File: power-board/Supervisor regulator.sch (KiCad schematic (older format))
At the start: 8 parts, among them U3 TPS7A4101

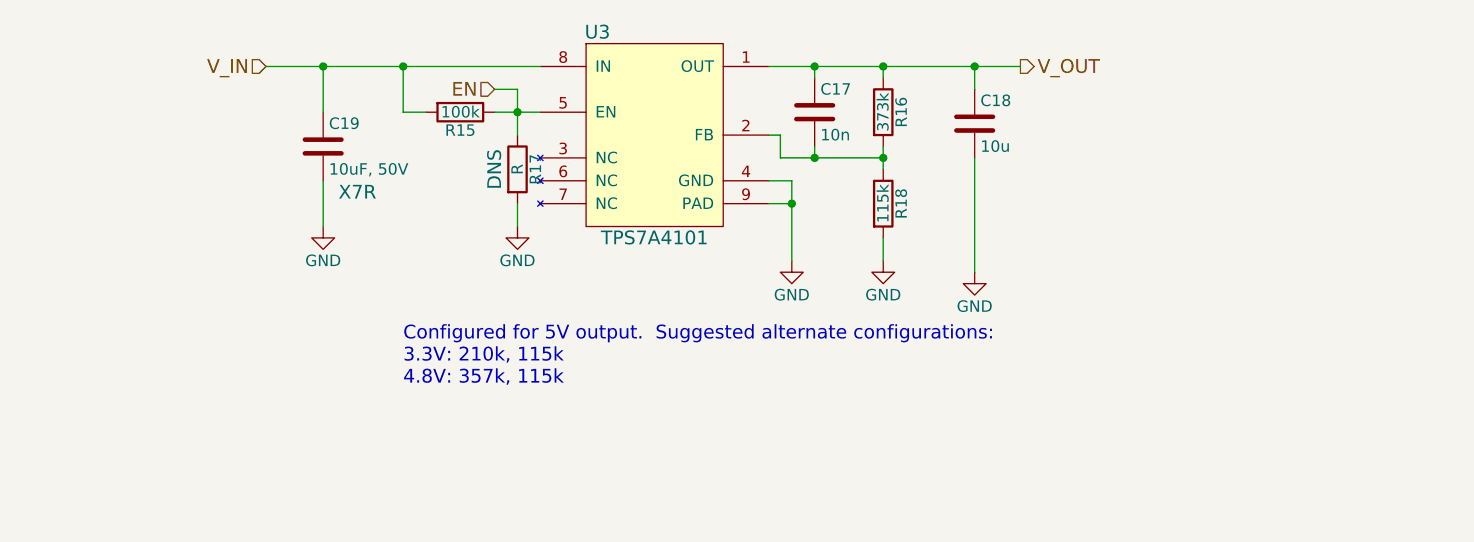
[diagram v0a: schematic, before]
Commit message: changed MCU to run at 3.3v
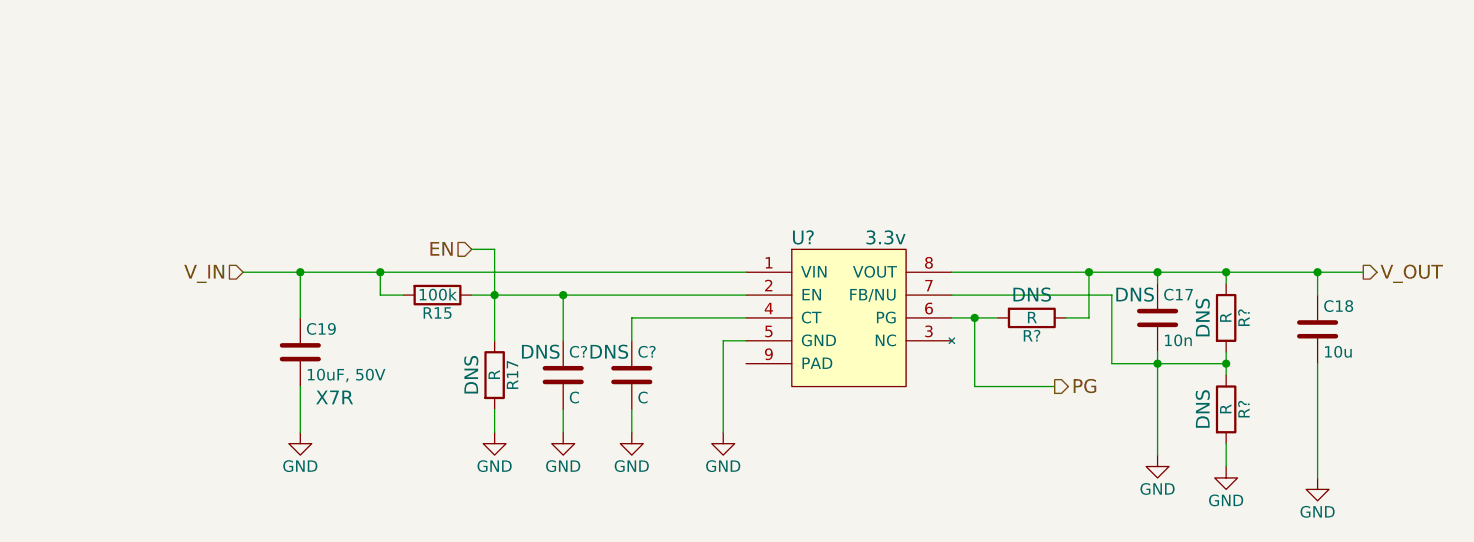
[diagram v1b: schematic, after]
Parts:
- removed R16: 373k, symbol R
- removed R18: 115k, symbol R
- removed U3: TPS7A4101, symbol TPS7A4101
- added C? (x2): C, symbol C
- added R? (x3): R, symbol R
- added U?: 3.3v, symbol TPS7A66xx-Q1
- C17: Note (none) -> DNS
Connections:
- net EN: now also C?.1, U?.2 (EN)
- net GND: now also C17.2, C?.2, C?.2, R?.1, R?.2, R?.2, U?.5 (GND), U?.7 (FB/NU)
- net V_IN: now also U?.1 (VIN)
- net V_OUT: now also R?.1, R?.1, U?.8 (VOUT)
- new net: C?.1, U?.4 (CT)
- new net PG: R?.2, U?.6 (PG)
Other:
- note removed: "Configured for 5V output. Suggested alternate configurations:\n3.3V: 210k, 115k\n4.8V: 357k, 115k"
- moved on the sheet: C17, C18, C19, R15, R17

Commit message: switched to XMEGA A4U
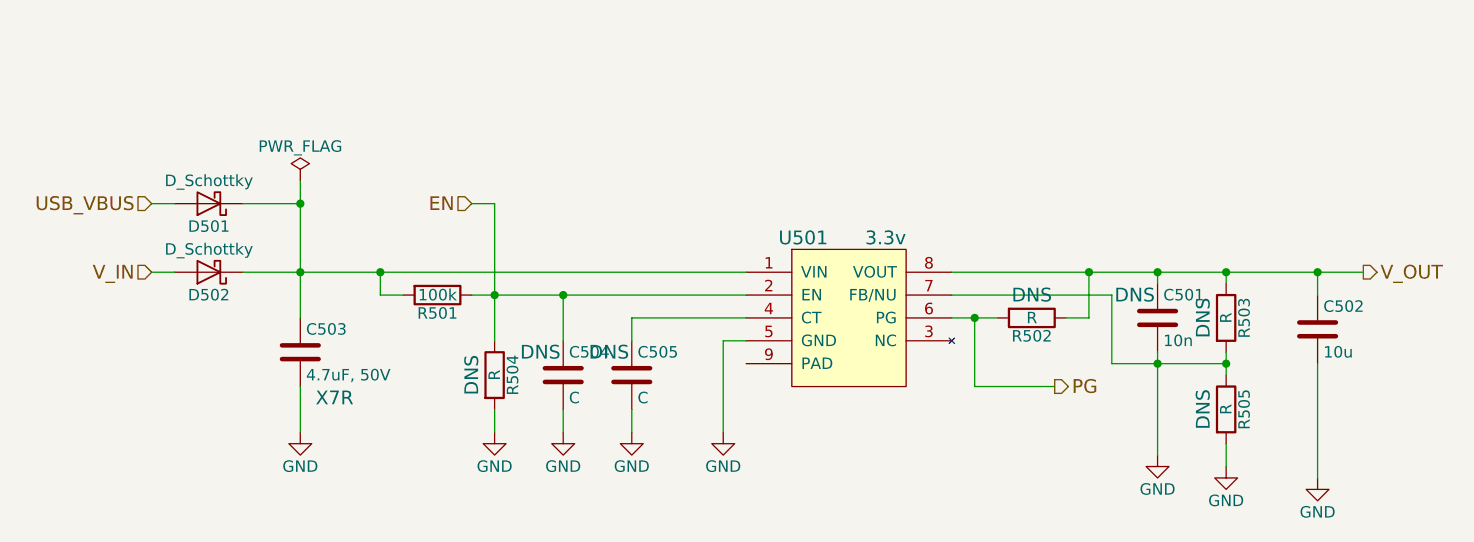
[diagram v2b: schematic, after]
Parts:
- added D501, D502: D_Schottky, symbol D_Schottky
- C503: renamed from C19; value 10uF, 50V -> 4.7uF, 50V; MFG Samsung -> (none); MPN CL31B106KBHNNNE -> (none)
- gave numbers to parts that had none: 6
- renumbered C17 to C501, C18 to C502, R15 to R501, R17 to R504
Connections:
- net V_IN: now also D502.2 (A); no longer C503.1, R501.2, U501.1 (VIN)
- new net: C503.1, D501.1 (K), D502.1 (K), R501.2, U501.1 (VIN)
- new net USB_VBUS: D501.2 (A)
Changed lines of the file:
@@
 $Descr A4 11693 8268
 encoding utf-8
-Sheet 5 10
+Sheet 5 11
 Title ""
 Date ""
@@
 Text HLabel 8100 3300 2    60   Output ~ 0
 V_OUT
-Text HLabel 3200 3300 0    60   Input ~ 0
+Text HLabel 2800 3300 0    60   Input ~ 0
 V_IN
 $Comp
-L C C19
+L C C503
 U 1 1 59357AE9
 P 3450 3650
-F 0 "C19" H 3475 3750 50  0000 L CNN
-F 1 "10uF, 50V" H 3475 3550 50  0000 L CNN
+F 0 "C503" H 3475 3750 50  0000 L CNN
+F 1 "4.7uF, 50V" H 3475 3550 50  0000 L CNN
 F 2 "" H 3488 3500 50  0000 C CNN
 F 3 "" H 3450 3650 50  0000 C CNN
 F 4 "X7R" H 3600 3450 60  0000 C CNN "Note"
-F 5 "Samsung" H 3450 3650 60  0001 C CNN "MFG"
-F 6 "CL31B106KBHNNNE" H 3450 3650 60  0001 C CNN "MPN"
 	1    3450 3650
 	1    0    0    -1
 $EndComp
 $Comp
-L C C17
+L C C501
 U 1 1 59357B30
 P 7200 3500
-F 0 "C17" H 7225 3600 50  0000 L CNN
+F 0 "C501" H 7225 3600 50  0000 L CNN
 F 1 "10n" H 7225 3400 50  0000 L CNN
 F 2 "" H 7238 3350 50  0000 C CNN
@@
 $EndComp
 $Comp
-L C C18
+L C C502
 U 1 1 59357B4B
 P 7900 3550
-F 0 "C18" H 7925 3650 50  0000 L CNN
+F 0 "C502" H 7925 3650 50  0000 L CNN
 F 1 "10u" H 7925 3450 50  0000 L CNN
 F 2 "" H 7938 3400 50  0000 C CNN
@@
 $EndComp
 $Comp
-L R R17
+L R R504
 U 1 1 59357FC8
 P 4300 3750
-F 0 "R17" V 4380 3750 50  0000 C CNN
+F 0 "R504" V 4380 3750 50  0000 C CNN
 F 1 "R" V 4300 3750 50  0000 C CNN
 F 2 "" V 4230 3750 50  0000 C CNN
@@
 Connection ~ 3800 3300
 Wire Wire Line
-	3450 3500 3450 3300
+	3450 2900 3450 3500
 Connection ~ 3450 3300
 Wire Wire Line
 	3450 3800 3450 4000
 $Comp
-L GND #PWR23
+L GND #PWR026
 U 1 1 59358101
 P 3450 4000
-F 0 "#PWR23" H 3450 3750 50  0001 C CNN
+F 0 "#PWR026" H 3450 3750 50  0001 C CNN
 F 1 "GND" H 3450 3850 50  0000 C CNN
 F 2 "" H 3450 4000 50  0000 C CNN
@@
 $EndComp
 $Comp
-L GND #PWR24
+L GND #PWR027
 U 1 1 59358125
 P 4300 4000
-F 0 "#PWR24" H 4300 3750 50  0001 C CNN
+F 0 "#PWR027" H 4300 3750 50  0001 C CNN
 F 1 "GND" H 4300 3850 50  0000 C CNN
 F 2 "" H 4300 4000 50  0000 C CNN
@@
 $EndComp
 $Comp
-L GND #PWR25
+L GND #PWR028
 U 1 1 59358149
 P 7200 4100
-F 0 "#PWR25" H 7200 3850 50  0001 C CNN
+F 0 "#PWR028" H 7200 3850 50  0001 C CNN
 F 1 "GND" H 7200 3950 50  0000 C CNN
 F 2 "" H 7200 4100 50  0000 C CNN
@@
 	7500 4050 7500 4150
 $Comp
-L GND #PWR26
+L GND #PWR029
 U 1 1 593583D2
 P 7500 4150
-F 0 "#PWR26" H 7500 3900 50  0001 C CNN
+F 0 "#PWR029" H 7500 3900 50  0001 C CNN
 F 1 "GND" H 7500 4000 50  0000 C CNN
 F 2 "" H 7500 4150 50  0000 C CNN
@@
 $EndComp
 $Comp
-L GND #PWR27
+L GND #PWR030
 U 1 1 59358405
 P 7900 4200
-F 0 "#PWR27" H 7900 3950 50  0001 C CNN
+F 0 "#PWR030" H 7900 3950 50  0001 C CNN
 F 1 "GND" H 7900 4050 50  0000 C CNN
 F 2 "" H 7900 4200 50  0000 C CNN
@@
 	7900 3400 7900 3300
 Connection ~ 7900 3300
-Text HLabel 4200 3200 0    60   Input ~ 0
+Text HLabel 4200 3000 0    60   Input ~ 0
 EN
 $Comp
-L R R15
+L R R501
 U 1 1 59357F3B
 P 4050 3400
-F 0 "R15" V 4130 3400 50  0000 C CNN
+F 0 "R501" V 4130 3400 50  0000 C CNN
 F 1 "100k" V 4050 3400 50  0000 C CNN
 F 2 "" V 3980 3400 50  0000 C CNN
@@
 $EndComp
 Wire Wire Line
-	4300 3200 4300 3600
-$Comp
-L C C?
+	4300 3000 4300 3600
+$Comp
+L C C505
 U 1 1 593B56C1
 P 4900 3750
-F 0 "C?" H 4925 3850 50  0000 L CNN
+F 0 "C505" H 4925 3850 50  0000 L CNN
 F 1 "C" H 4925 3650 50  0000 L CNN
 F 2 "" H 4938 3600 50  0001 C CNN
@@
 	5300 3600 5400 3600
 $Comp
-L GND #PWR?
+L GND #PWR031
 U 1 1 593B586D
 P 4900 4000
-F 0 "#PWR?" H 4900 3750 50  0001 C CNN
+F 0 "#PWR031" H 4900 3750 50  0001 C CNN
 F 1 "GND" H 4900 3850 50  0000 C CNN
 F 2 "" H 4900 4000 50  0000 C CNN
@@
 $EndComp
 $Comp
-L TPS7A66xx-Q1 U?
+L TPS7A66xx-Q1 U501
 U 1 1 593B5C53
 P 5600 3200
-F 0 "U?" H 5650 3250 60  0000 C CNN
+F 0 "U501" H 5650 3250 60  0000 C CNN
 F 1 "3.3v" H 6100 3250 60  0000 R CNN
 F 2 "" H 6950 1800 60  0001 C CNN
@@
 $EndComp
 $Comp
-L GND #PWR?
+L GND #PWR032
 U 1 1 593B5D2B
 P 5300 4000
-F 0 "#PWR?" H 5300 3750 50  0001 C CNN
+F 0 "#PWR032" H 5300 3750 50  0001 C CNN
 F 1 "GND" H 5300 3850 50  0000 C CNN
 F 2 "" H 5300 4000 50  0000 C CNN
@@
 $EndComp
 Wire Wire Line
-	4200 3200 4300 3200
-$Comp
-L R R?
+	4200 3000 4300 3000
+$Comp
+L R R503
 U 1 1 593B5FF1
 P 7500 3500
-F 0 "R?" V 7580 3500 50  0000 C CNN
+F 0 "R503" V 7580 3500 50  0000 C CNN
 F 1 "R" V 7500 3500 50  0000 C CNN
 F 2 "" V 7430 3500 50  0000 C CNN
@@
 $EndComp
 $Comp
-L R R?
+L R R505
 U 1 1 593B60BB
 P 7500 3900
-F 0 "R?" V 7580 3900 50  0000 C CNN
+F 0 "R505" V 7580 3900 50  0000 C CNN
 F 1 "R" V 7500 3900 50  0000 C CNN
 F 2 "" V 7430 3900 50  0000 C CNN
@@
 	7000 3400 7000 3700
 $Comp
-L R R?
+L R R502
 U 1 1 593B61E2
 P 6650 3500
-F 0 "R?" V 6730 3500 50  0000 C CNN
+F 0 "R502" V 6730 3500 50  0000 C CNN
 F 1 "R" V 6650 3500 50  0000 C CNN
 F 2 "" V 6580 3500 50  0000 C CNN
@@
 PG
 $Comp
-L C C?
+L C C504
 U 1 1 593B702A
 P 4600 3750
-F 0 "C?" H 4625 3850 50  0000 L CNN
+F 0 "C504" H 4625 3850 50  0000 L CNN
 F 1 "C" H 4625 3650 50  0000 L CNN
 F 2 "" H 4638 3600 50  0001 C CNN
@@
 	4600 3900 4600 4000
 $Comp
-L GND #PWR?
+L GND #PWR033
 U 1 1 593B7154
 P 4600 4000
-F 0 "#PWR?" H 4600 3750 50  0001 C CNN
+F 0 "#PWR033" H 4600 3750 50  0001 C CNN
 F 1 "GND" H 4600 3850 50  0000 C CNN
 F 2 "" H 4600 4000 50  0000 C CNN
@@
 	1    0    0    -1
 $EndComp
+Text HLabel 2800 3000 0    60   Input ~ 0
+USB_VBUS
+$Comp
+L D_Schottky D501
+U 1 1 593D7594
+P 3050 3000
+F 0 "D501" H 3050 3100 50  0000 C CNN
+F 1 "D_Schottky" H 3050 2900 50  0000 C CNN
+F 2 "" H 3050 3000 50  0001 C CNN
+F 3 "" H 3050 3000 50  0001 C CNN
+	1    3050 3000
+	-1   0    0    1
+$EndComp
+$Comp
+L D_Schottky D502
+U 1 1 593D75D5
+P 3050 3300
+F 0 "D502" H 3050 3400 50  0000 C CNN
+F 1 "D_Schottky" H 3050 3200 50  0000 C CNN
+F 2 "" H 3050 3300 50  0001 C CNN
+F 3 "" H 3050 3300 50  0001 C CNN
+	1    3050 3300
+	-1   0    0    1
+$EndComp
+Wire Wire Line
+	2800 3000 2900 3000
+Wire Wire Line
+	2900 3300 2800 3300
+Wire Wire Line
+	3200 3000 3450 3000
+$Comp
+L PWR_FLAG #FLG034
+U 1 1 593DC019
+P 3450 2900
+F 0 "#FLG034" H 3450 2975 50  0001 C CNN
+F 1 "PWR_FLAG" H 3450 3050 50  0000 C CNN
+F 2 "" H 3450 2900 50  0001 C CNN
+F 3 "" H 3450 2900 50  0001 C CNN
+	1    3450 2900
+	1    0    0    -1
+$EndComp
+Connection ~ 3450 3000
 $EndSCHEMATC

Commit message: routed board
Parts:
- removed D501, D502: D_Schottky, symbol D_Schottky
- added D501: MMBD1204, TO_SOT_Packages_SMD:SOT-23, symbol D_Schottky_x2_KCom_AAK
- C501, C504: footprint (none) -> Capacitors_SMD:C_0603
- C502: value 10u -> 47u; footprint (none) -> Capacitors_SMD:C_0805; MFG Samsung -> Taiyo Yuden; MPN CL21A106KOQNNNG -> JMK212BBJ476MG-T
- C503: footprint (none) -> Capacitors_SMD:C_0805; MFG (none) -> Samsung; MPN (none) -> CL21A475KQFNNNG
- C505: footprint (none) -> Capacitors_SMD:C_0805
- R501: footprint (none) -> Resistors_SMD:R_0603; MFG Vishay / Draloric -> Yageo; MPN RCA0603100KJNEC -> RC0603JR-07100KL
- R502, R504: footprint (none) -> Resistors_SMD:R_0603
- R503, R505: footprint (none) -> Resistors_SMD:R_0805
- U501: footprint (none) -> Housings_SSOP:MSOP-8-1EP_3x3mm_Pitch0.65mm
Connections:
- net GND: now also U501.9 (PAD); no longer C501.2, R503.2, R505.1, U501.7 (FB/NU)
- net USB_VBUS: now also D501.1 (A)
- net V_IN: now also D501.2 (A)
- net at C503.1, R501.2, U501.1 (VIN): now also D501.3 (K)
- new net: C501.2, R503.2, R505.1, U501.7 (FB/NU)
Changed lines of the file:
@@
 $Descr A4 11693 8268
 encoding utf-8
-Sheet 5 11
+Sheet 4 12
 Title ""
 Date ""
@@
 Text HLabel 8100 3300 2    60   Output ~ 0
 V_OUT
-Text HLabel 2800 3300 0    60   Input ~ 0
+Text HLabel 2900 2900 0    60   Input ~ 0
 V_IN
 $Comp
@@
 F 0 "C503" H 3475 3750 50  0000 L CNN
 F 1 "4.7uF, 50V" H 3475 3550 50  0000 L CNN
-F 2 "" H 3488 3500 50  0000 C CNN
+F 2 "Capacitors_SMD:C_0805" H 3488 3500 50  0001 C CNN
 F 3 "" H 3450 3650 50  0000 C CNN
 F 4 "X7R" H 3600 3450 60  0000 C CNN "Note"
+F 5 "Samsung" H 3450 3650 60  0001 C CNN "MFG"
+F 6 "CL21A475KQFNNNG" H 3450 3650 60  0001 C CNN "MPN"
 	1    3450 3650
 	1    0    0    -1
@@
 F 0 "C501" H 7225 3600 50  0000 L CNN
 F 1 "10n" H 7225 3400 50  0000 L CNN
-F 2 "" H 7238 3350 50  0000 C CNN
+F 2 "Capacitors_SMD:C_0603" H 7238 3350 50  0001 C CNN
 F 3 "" H 7200 3500 50  0000 C CNN
 F 4 "Murata Electronics" H 7200 3500 60  0001 C CNN "MFG"
@@
 P 7900 3550
 F 0 "C502" H 7925 3650 50  0000 L CNN
-F 1 "10u" H 7925 3450 50  0000 L CNN
-F 2 "" H 7938 3400 50  0000 C CNN
+F 1 "47u" H 7925 3450 50  0000 L CNN
+F 2 "Capacitors_SMD:C_0805" H 7938 3400 50  0001 C CNN
 F 3 "" H 7900 3550 50  0000 C CNN
-F 4 "Samsung" H 7900 3550 60  0001 C CNN "MFG"
-F 5 "CL21A106KOQNNNG" H 7900 3550 60  0001 C CNN "MPN"
+F 4 "Taiyo Yuden" H 7900 3550 60  0001 C CNN "MFG"
+F 5 "JMK212BBJ476MG-T" H 7900 3550 60  0001 C CNN "MPN"
 	1    7900 3550
 	1    0    0    -1
@@
 F 0 "R504" V 4380 3750 50  0000 C CNN
 F 1 "R" V 4300 3750 50  0000 C CNN
-F 2 "" V 4230 3750 50  0000 C CNN
+F 2 "Resistors_SMD:R_0603" V 4230 3750 50  0001 C CNN
 F 3 "" H 4300 3750 50  0000 C CNN
 F 4 "DNS" V 4200 3750 60  0000 C CNN "Note"
@@
 Connection ~ 3800 3300
 Wire Wire Line
-	3450 2900 3450 3500
+	3450 3200 3450 3500
 Connection ~ 3450 3300
 Wire Wire Line
 	3450 3800 3450 4000
 $Comp
-L GND #PWR026
+L GND #PWR013
 U 1 1 59358101
 P 3450 4000
-F 0 "#PWR026" H 3450 3750 50  0001 C CNN
+F 0 "#PWR013" H 3450 3750 50  0001 C CNN
 F 1 "GND" H 3450 3850 50  0000 C CNN
 F 2 "" H 3450 4000 50  0000 C CNN
@@
 $EndComp
 $Comp
-L GND #PWR027
+L GND #PWR014
 U 1 1 59358125
 P 4300 4000
-F 0 "#PWR027" H 4300 3750 50  0001 C CNN
+F 0 "#PWR014" H 4300 3750 50  0001 C CNN
 F 1 "GND" H 4300 3850 50  0000 C CNN
 F 2 "" H 4300 4000 50  0000 C CNN
@@
 	1    0    0    -1
 $EndComp
-$Comp
-L GND #PWR028
-U 1 1 59358149
-P 7200 4100
-F 0 "#PWR028" H 7200 3850 50  0001 C CNN
-F 1 "GND" H 7200 3950 50  0000 C CNN
-F 2 "" H 7200 4100 50  0000 C CNN
-F 3 "" H 7200 4100 50  0000 C CNN
-	1    7200 4100
-	1    0    0    -1
-$EndComp
 Wire Wire Line
 	6300 3300 8100 3300
@@
 Connection ~ 7200 3300
 Wire Wire Line
-	7200 3650 7200 4100
-Wire Wire Line
 	7500 4050 7500 4150
 $Comp
-L GND #PWR029
+L GND #PWR015
 U 1 1 593583D2
 P 7500 4150
-F 0 "#PWR029" H 7500 3900 50  0001 C CNN
+F 0 "#PWR015" H 7500 3900 50  0001 C CNN
 F 1 "GND" H 7500 4000 50  0000 C CNN
 F 2 "" H 7500 4150 50  0000 C CNN
@@
 $EndComp
 $Comp
-L GND #PWR030
+L GND #PWR016
 U 1 1 59358405
 P 7900 4200
-F 0 "#PWR030" H 7900 3950 50  0001 C CNN
+F 0 "#PWR016" H 7900 3950 50  0001 C CNN
 F 1 "GND" H 7900 4050 50  0000 C CNN
 F 2 "" H 7900 4200 50  0000 C CNN
@@
 F 0 "R501" V 4130 3400 50  0000 C CNN
 F 1 "100k" V 4050 3400 50  0000 C CNN
-F 2 "" V 3980 3400 50  0000 C CNN
+F 2 "Resistors_SMD:R_0603" V 3980 3400 50  0001 C CNN
 F 3 "" H 4050 3400 50  0000 C CNN
-F 4 "Vishay / Draloric" V 4050 3400 60  0001 C CNN "MFG"
-F 5 "RCA0603100KJNEC" V 4050 3400 60  0001 C CNN "MPN"
+F 4 "Yageo" V 4050 3400 60  0001 C CNN "MFG"
+F 5 "RC0603JR-07100KL" V 4050 3400 60  0001 C CNN "MPN"
 	1    4050 3400
 	0    1    1    0
@@
 F 0 "C505" H 4925 3850 50  0000 L CNN
 F 1 "C" H 4925 3650 50  0000 L CNN
-F 2 "" H 4938 3600 50  0001 C CNN
+F 2 "Capacitors_SMD:C_0805" H 4938 3600 50  0001 C CNN
 F 3 "" H 4900 3750 50  0001 C CNN
 F 4 "DNS" H 4800 3850 60  0000 C CNN "Note"
@@
 	5300 3600 5400 3600
 $Comp
-L GND #PWR031
+L GND #PWR017
 U 1 1 593B586D
 P 4900 4000
-F 0 "#PWR031" H 4900 3750 50  0001 C CNN
+F 0 "#PWR017" H 4900 3750 50  0001 C CNN
 F 1 "GND" H 4900 3850 50  0000 C CNN
 F 2 "" H 4900 4000 50  0000 C CNN
@@
 F 0 "U501" H 5650 3250 60  0000 C CNN
 F 1 "3.3v" H 6100 3250 60  0000 R CNN
-F 2 "" H 6950 1800 60  0001 C CNN
+F 2 "Housings_SSOP:MSOP-8-1EP_3x3mm_Pitch0.65mm" H 6950 1800 60  0001 C CNN
 F 3 "" H 6950 1800 60  0001 C CNN
 F 4 "Texas Instruments" H 5750 3350 60  0001 C CNN "MFG"
@@
 $EndComp
 $Comp
-L GND #PWR032
+L GND #PWR018
 U 1 1 593B5D2B
 P 5300 4000
-F 0 "#PWR032" H 5300 3750 50  0001 C CNN
+F 0 "#PWR018" H 5300 3750 50  0001 C CNN
 F 1 "GND" H 5300 3850 50  0000 C CNN
 F 2 "" H 5300 4000 50  0000 C CNN
@@
 F 0 "R503" V 7580 3500 50  0000 C CNN
 F 1 "R" V 7500 3500 50  0000 C CNN
-F 2 "" V 7430 3500 50  0000 C CNN
+F 2 "Resistors_SMD:R_0805" V 7430 3500 50  0001 C CNN
 F 3 "" H 7500 3500 50  0000 C CNN
 F 4 "DNS" V 7400 3500 60  0000 C CNN "Note"
@@
 F 0 "R505" V 7580 3900 50  0000 C CNN
 F 1 "R" V 7500 3900 50  0000 C CNN
-F 2 "" V 7430 3900 50  0000 C CNN
+F 2 "Resistors_SMD:R_0805" V 7430 3900 50  0001 C CNN
 F 3 "" H 7500 3900 50  0000 C CNN
 F 4 "DNS" V 7400 3900 60  0000 C CNN "Note"
@@
 F 0 "R502" V 6730 3500 50  0000 C CNN
 F 1 "R" V 6650 3500 50  0000 C CNN
-F 2 "" V 6580 3500 50  0000 C CNN
+F 2 "Resistors_SMD:R_0603" V 6580 3500 50  0001 C CNN
 F 3 "" H 6650 3500 50  0000 C CNN
 F 4 "DNS" V 6550 3500 60  0000 C CNN "Note"
@@
 F 0 "C504" H 4625 3850 50  0000 L CNN
 F 1 "C" H 4625 3650 50  0000 L CNN
-F 2 "" H 4638 3600 50  0001 C CNN
+F 2 "Capacitors_SMD:C_0603" H 4638 3600 50  0001 C CNN
 F 3 "" H 4600 3750 50  0001 C CNN
 F 4 "DNS" H 4500 3850 60  0000 C CNN "Note"
@@
 	4600 3900 4600 4000
 $Comp
-L GND #PWR033
+L GND #PWR019
 U 1 1 593B7154
 P 4600 4000
-F 0 "#PWR033" H 4600 3750 50  0001 C CNN
+F 0 "#PWR019" H 4600 3750 50  0001 C CNN
 F 1 "GND" H 4600 3850 50  0000 C CNN
 F 2 "" H 4600 4000 50  0000 C CNN
@@
 	1    0    0    -1
 $EndComp
-Text HLabel 2800 3000 0    60   Input ~ 0
+Text HLabel 2900 3700 0    60   Input ~ 0
 USB_VBUS
-$Comp
-L D_Schottky D501
-U 1 1 593D7594
-P 3050 3000
-F 0 "D501" H 3050 3100 50  0000 C CNN
-F 1 "D_Schottky" H 3050 2900 50  0000 C CNN
-F 2 "" H 3050 3000 50  0001 C CNN
-F 3 "" H 3050 3000 50  0001 C CNN
-	1    3050 3000
-	-1   0    0    1
-$EndComp
-$Comp
-L D_Schottky D502
-U 1 1 593D75D5
-P 3050 3300
-F 0 "D502" H 3050 3400 50  0000 C CNN
-F 1 "D_Schottky" H 3050 3200 50  0000 C CNN
-F 2 "" H 3050 3300 50  0001 C CNN
-F 3 "" H 3050 3300 50  0001 C CNN
-	1    3050 3300
-	-1   0    0    1
-$EndComp
-Wire Wire Line
-	2800 3000 2900 3000
-Wire Wire Line
-	2900 3300 2800 3300
-Wire Wire Line
-	3200 3000 3450 3000
-$Comp
-L PWR_FLAG #FLG034
+Wire Wire Line
+	2900 2900 3000 2900
+Wire Wire Line
+	3000 3700 2900 3700
+$Comp
+L PWR_FLAG #FLG020
 U 1 1 593DC019
-P 3450 2900
-F 0 "#FLG034" H 3450 2975 50  0001 C CNN
-F 1 "PWR_FLAG" H 3450 3050 50  0000 C CNN
-F 2 "" H 3450 2900 50  0001 C CNN
-F 3 "" H 3450 2900 50  0001 C CNN
-	1    3450 2900
-	1    0    0    -1
-$EndComp
-Connection ~ 3450 3000
+P 3450 3200
+F 0 "#FLG020" H 3450 3275 50  0001 C CNN
+F 1 "PWR_FLAG" H 3450 3350 50  0000 C CNN
+F 2 "" H 3450 3200 50  0001 C CNN
+F 3 "" H 3450 3200 50  0001 C CNN
+	1    3450 3200
+	1    0    0    -1
+$EndComp
+$Comp
+L D_Schottky_x2_KCom_AAK D501
+U 1 1 593E632A
+P 3000 3300
+F 0 "D501" H 3050 3200 50  0000 C CNN
+F 1 "MMBD1204" H 3000 3400 50  0000 C CNN
+F 2 "TO_SOT_Packages_SMD:SOT-23" H 3000 3300 50  0001 C CNN
+F 3 "" H 3000 3300 50  0001 C CNN
+F 4 "Fairchild/ON Semiconductor" H 3000 3300 60  0001 C CNN "MFG"
+F 5 "MMBD1204" H 3000 3300 60  0001 C CNN "MPN"
+	1    3000 3300
+	0    -1   -1   0
+$EndComp
+Wire Wire Line
+	3000 2900 3000 3000
+Wire Wire Line
+	3000 3600 3000 3700
+Wire Wire Line
+	5400 3700 5300 3700
+Connection ~ 5300 3700
+Wire Wire Line
+	7200 3700 7200 3650
 $EndSCHEMATC

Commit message: adding more part numbers
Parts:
- R504: MFG (none) -> Yageo; MPN (none) -> RC0603JR-070RL
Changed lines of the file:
@@
 F 3 "" H 4300 3750 50  0000 C CNN
 F 4 "DNS" V 4200 3750 60  0000 C CNN "Note"
+F 5 "Yageo" V 4300 3750 60  0001 C CNN "MFG"
+F 6 "RC0603JR-070RL" V 4300 3750 60  0001 C CNN "MPN"
 	1    4300 3750
 	1    0    0    -1
@@
 Wire Wire Line
 	7000 3400 7000 3700
-$Comp
-L R R502
-U 1 1 593B61E2
-P 6650 3500
-F 0 "R502" V 6730 3500 50  0000 C CNN
-F 1 "R" V 6650 3500 50  0000 C CNN
-F 2 "Resistors_SMD:R_0603" V 6580 3500 50  0001 C CNN
-F 3 "" H 6650 3500 50  0000 C CNN
-F 4 "DNS" V 6550 3500 60  0000 C CNN "Note"
-	1    6650 3500
-	0    1    1    0
-$EndComp
 Wire Wire Line
 	6800 3500 6900 3500
@@
 Wire Wire Line
 	7200 3700 7200 3650
+$Comp
+L R R502
+U 1 1 593B61E2
+P 6650 3500
+F 0 "R502" V 6730 3500 50  0000 C CNN
+F 1 "R" V 6650 3500 50  0000 C CNN
+F 2 "Resistors_SMD:R_0603" V 6580 3500 50  0001 C CNN
+F 3 "" H 6650 3500 50  0000 C CNN
+F 4 "DNS" V 6550 3500 60  0000 C CNN "Note"
+	1    6650 3500
+	0    1    1    0
+$EndComp
 $EndSCHEMATC
